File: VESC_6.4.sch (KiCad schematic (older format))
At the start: 23 parts, among them J1 CAN, J2 HALL_ENC, J3 COMM, J4 SERVO, J5 SWD, J6 USB_OTG, SW1 SENSOR_VOLTAGE

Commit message: lots of PCB work
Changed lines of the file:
@@
 F25 "GH_B" I R 8400 2800 60
 F26 "GL_B" I R 8400 3000 60
-F27 "SL_B" I L 7150 3750 60
+F27 "SL_B" I R 8400 3100 60
 F28 "GH_C" I R 8400 3300 60
 F29 "GL_C" I R 8400 3500 60

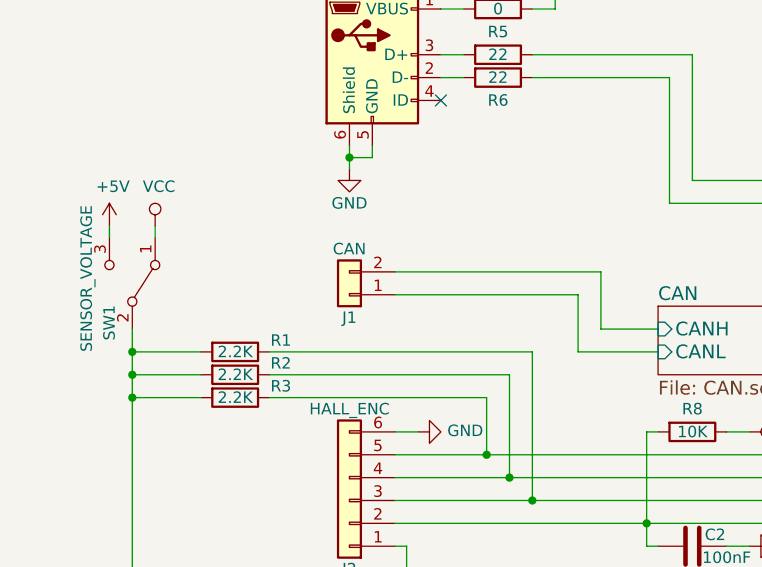
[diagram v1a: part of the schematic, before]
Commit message: changed the USB port around added CAD stuff
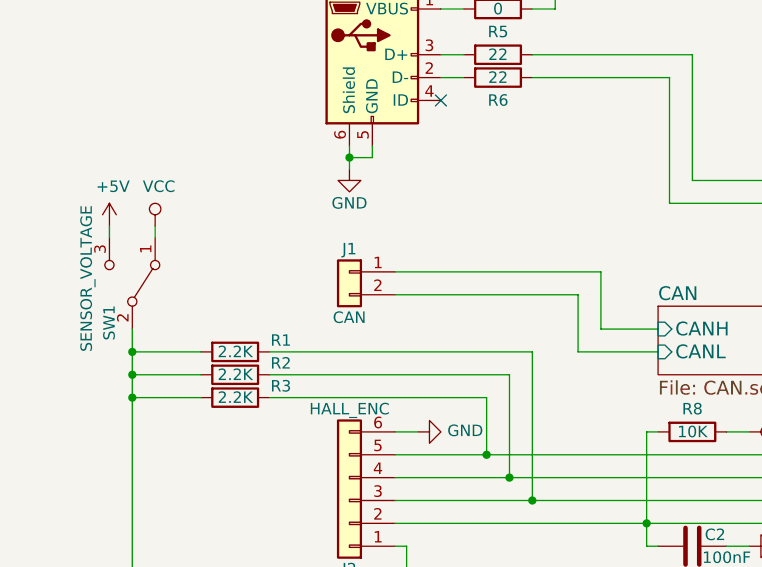
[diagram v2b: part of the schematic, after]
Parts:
- J6: footprint Connectors_USB:USB_Micro-B_Vertical_Molex-105133-0001 -> Connector_USB:USB_Micro-B_Molex-105017-0001
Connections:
- net CAN/CANH: now also J1.1 (Pin_1); no longer J1.2 (Pin_2)
- net CAN/CANL: now also J1.2 (Pin_2); no longer J1.1 (Pin_1)
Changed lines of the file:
@@
 L Conn_01x02 J1
 U 1 1 5A7A021D
-P 2300 2350
-F 0 "J1" H 2300 2450 50  0000 C CNN
-F 1 "CAN" H 2300 2150 50  0000 C CNN
-F 2 "Connectors_JST:JST_PH_B2B-PH-K_02x2.00mm_Straight" H 2300 2350 50  0001 C CNN
-F 3 "" H 2300 2350 50  0001 C CNN
-	1    2300 2350
-	-1   0    0    1
+P 2300 2250
+F 0 "J1" H 2300 2350 50  0000 C CNN
+F 1 "CAN" H 2300 2050 50  0000 C CNN
+F 2 "Connectors_JST:JST_PH_B2B-PH-K_02x2.00mm_Straight" H 2300 2250 50  0001 C CNN
+F 3 "" H 2300 2250 50  0001 C CNN
+	1    2300 2250
+	-1   0    0    -1
 $EndComp
 Wire Wire Line
@@
 F 0 "J6" H 2455 1767 50  0000 C CNN
 F 1 "USB_OTG" H 2455 1676 50  0000 C CNN
-F 2 "Connectors_USB:USB_Micro-B_Vertical_Molex-105133-0001" H 2550 1250 50  0001 C CNN
+F 2 "Connector_USB:USB_Micro-B_Molex-105017-0001" H 2550 1250 50  0001 C CNN
 F 3 "" H 2550 1250 50  0001 C CNN
 	1    2400 1300

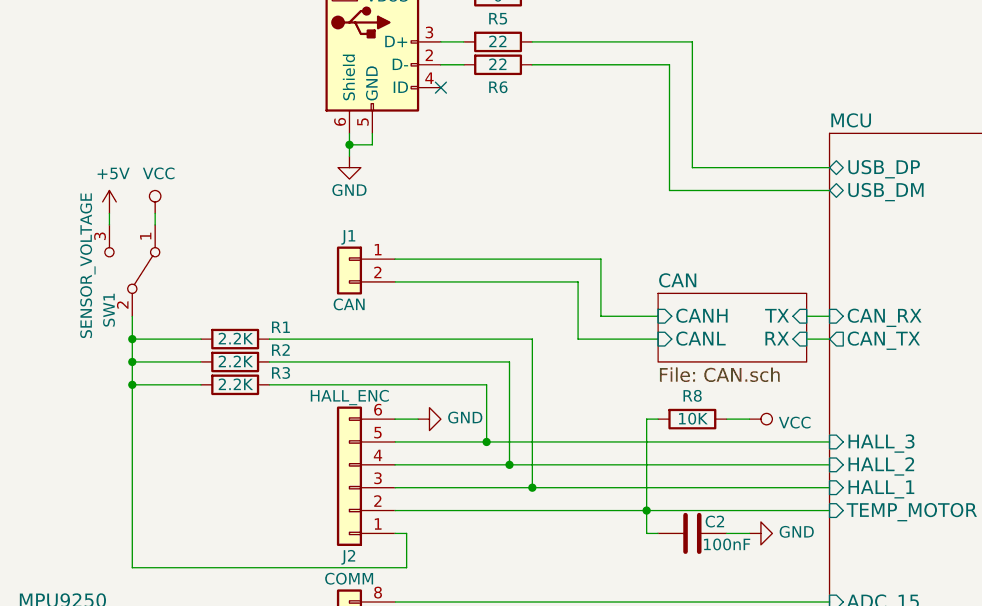
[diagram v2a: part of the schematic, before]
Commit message: removed 5v/3v3 sensor switch
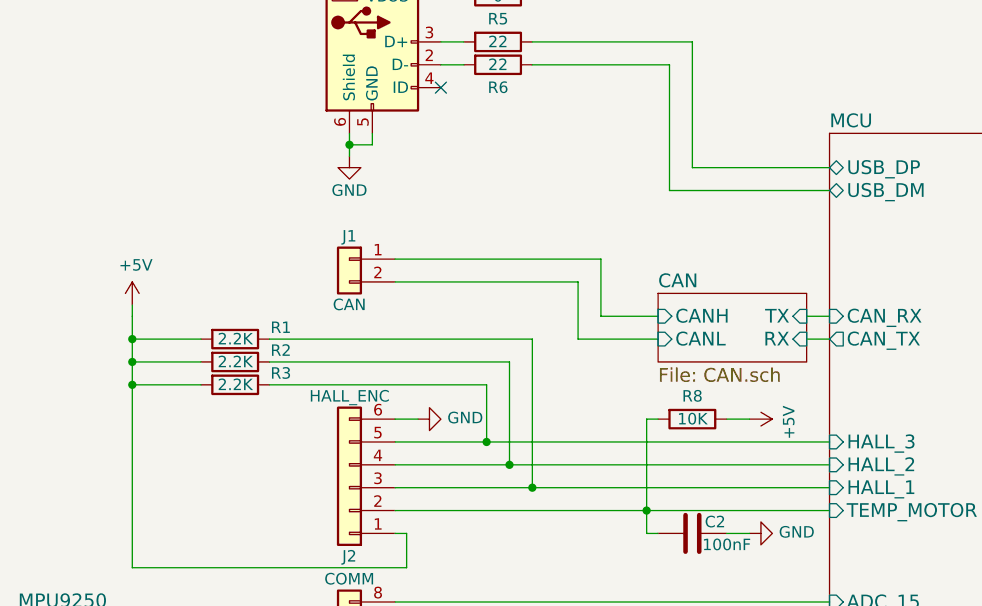
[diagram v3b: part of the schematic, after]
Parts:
- removed SW1: SENSOR_VOLTAGE, Global_Parts:JS102011JCQN, symbol SW_SPDT
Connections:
- net +5V: now also J2.1 (Pin_1), R1.2, R2.2, R3.2, R8.1
- net VCC: no longer R8.1
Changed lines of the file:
@@
-$EndComp
-$Comp
-L VCC #PWR019
-U 1 1 5A7960F2
-P 4050 2950
-F 0 "#PWR019" H 4050 2800 50  0001 C CNN
-F 1 "VCC" V 4067 3078 50  0000 L CNN
-F 2 "" H 4050 2950 50  0001 C CNN
-F 3 "" H 4050 2950 50  0001 C CNN
-	1    4050 2950
-	0    1    1    0
 $EndComp
 $Comp
@@
 $EndComp
 $Comp
-L SW_SPDT SW1
-U 1 1 5A79C7B9
-P 1350 2300
-F 0 "SW1" H 1100 2200 50  0000 L CNN
-F 1 "SENSOR_VOLTAGE" H 1050 2100 50  0000 L CNN
-F 2 "Global_Parts:JS102011JCQN" H 1350 2300 50  0001 C CNN
-F 3 "" H 1350 2300 50  0001 C CNN
-	1    1350 2300
-	0    1    -1   0
-$EndComp
-$Comp
-L VCC #PWR02
-U 1 1 5A79CD83
-P 1450 2050
-F 0 "#PWR02" H 1450 1900 50  0001 C CNN
-F 1 "VCC" H 1467 2223 50  0000 C CNN
-F 2 "" H 1450 2050 50  0001 C CNN
-F 3 "" H 1450 2050 50  0001 C CNN
-	1    1450 2050
-	1    0    0    -1
-$EndComp
-$Comp
 L +5V #PWR01
 U 1 1 5A79D04F
-P 1250 2050
-F 0 "#PWR01" H 1250 1900 50  0001 C CNN
-F 1 "+5V" H 1265 2223 50  0000 C CNN
-F 2 "" H 1250 2050 50  0001 C CNN
-F 3 "" H 1250 2050 50  0001 C CNN
-	1    1250 2050
+P 1350 2450
+F 0 "#PWR01" H 1350 2300 50  0001 C CNN
+F 1 "+5V" H 1365 2623 50  0000 C CNN
+F 2 "" H 1350 2450 50  0001 C CNN
+F 3 "" H 1350 2450 50  0001 C CNN
+	1    1350 2450
 	1    0    0    -1
 $EndComp
@@
 Connection ~ 1350 2800
 Wire Wire Line
-	1450 2050 1450 2100
-Wire Wire Line
-	1250 2050 1250 2100
+	1350 2450 1350 2500
 Wire Wire Line
 	4300 2600 4400 2600
@@
 Wire Wire Line
 	8900 1800 8400 1800
+$Comp
+L +5V #PWR?
+U 1 1 5AC9A53F
+P 4050 2950
+F 0 "#PWR?" H 4050 2800 50  0001 C CNN
+F 1 "+5V" H 4065 3123 50  0000 C CNN
+F 2 "" H 4050 2950 50  0001 C CNN
+F 3 "" H 4050 2950 50  0001 C CNN
+	1    4050 2950
+	0    1    1    0
+$EndComp
 $EndSCHEMATC

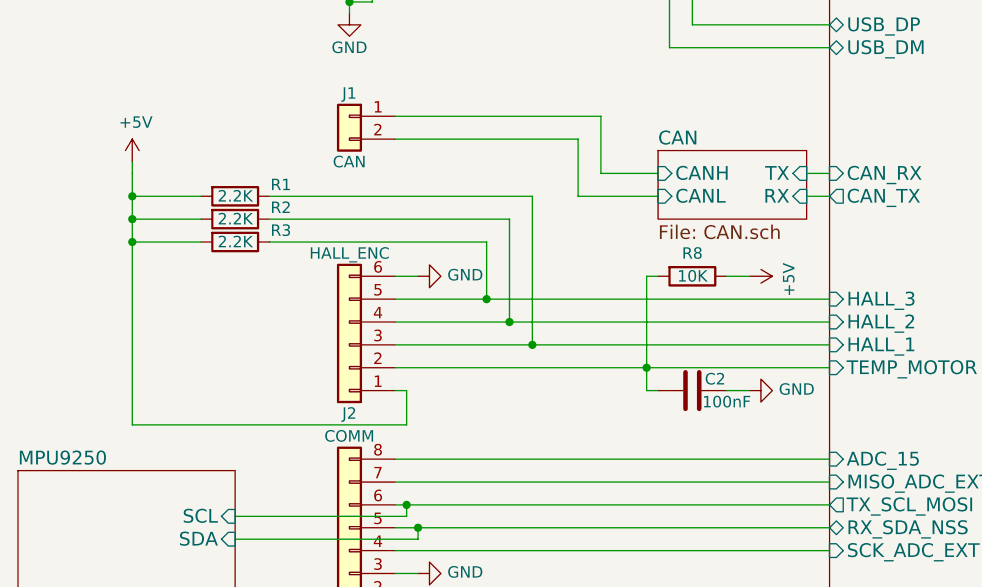
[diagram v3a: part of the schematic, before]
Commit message: removed sensor switch
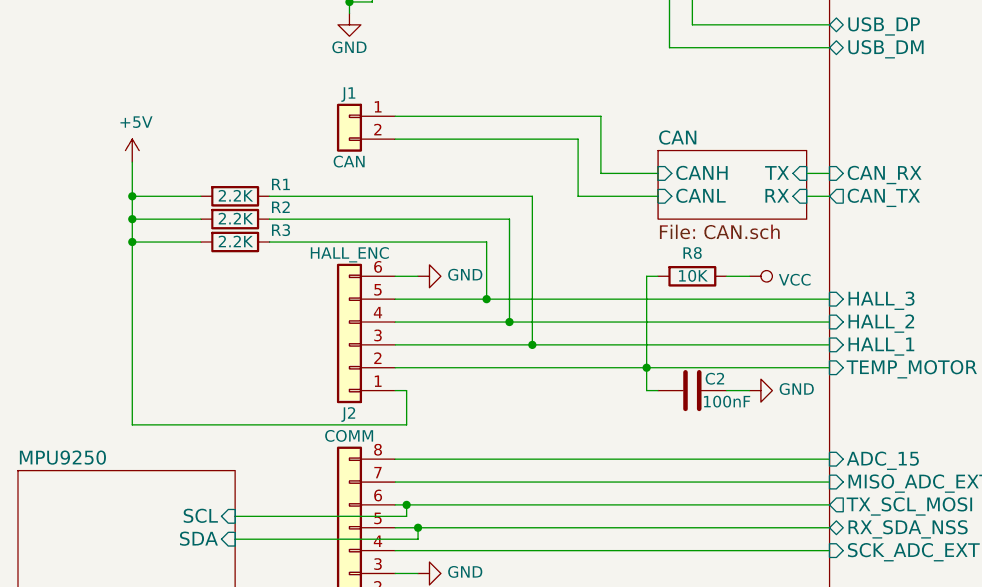
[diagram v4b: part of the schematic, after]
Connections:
- net +5V: no longer R8.1
- net VCC: now also R8.1
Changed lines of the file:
@@
 	2550 3450 2550 3600
 Wire Wire Line
-	2550 3600 1350 3600
-Wire Wire Line
-	1350 3600 1350 2500
+	1350 3600 2550 3600
+Wire Wire Line
+	1350 2450 1350 3600
 Wire Wire Line
 	2500 3350 4400 3350
@@
 	1650 2800 1350 2800
 Connection ~ 1350 2800
-Wire Wire Line
-	1350 2450 1350 2500
 Wire Wire Line
 	4300 2600 4400 2600
@@
 	8900 1800 8400 1800
 $Comp
-L +5V #PWR?
-U 1 1 5AC9A53F
+L VCC #PWR02
+U 1 1 5ACEC4D9
 P 4050 2950
-F 0 "#PWR?" H 4050 2800 50  0001 C CNN
-F 1 "+5V" H 4065 3123 50  0000 C CNN
+F 0 "#PWR02" H 4050 2800 50  0001 C CNN
+F 1 "VCC" V 4067 3078 50  0000 L CNN
 F 2 "" H 4050 2950 50  0001 C CNN
 F 3 "" H 4050 2950 50  0001 C CNN
